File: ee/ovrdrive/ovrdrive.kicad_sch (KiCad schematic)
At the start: 48 parts, among them J1 USB_A, J2 Conn_01x02_Female, Q1 RU1J002YNTCL, U1 SM3257ENT, U2 FLASH, U3 ATtiny24A-MM, U4 74AUC1G32, U5 LMV321, U6 LM4040DBZ-2.5

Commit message: Added some datasheets made some changes to the boards.
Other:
- note removed: "Open Questions 1. Where does DQS0 from U1 wire to? 2. U1-P44, wired to 680R resistor in design guide."
- moved on the sheet: C18
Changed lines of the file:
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@@
     (stroke (width 0) (type default) (color 0 0 0 0))
   )
-  (wire (pts (xy 204.47 81.915) (xy 204.47 82.55))
+  (wire (pts (xy 213.36 80.645) (xy 213.36 81.28))
     (stroke (width 0) (type default) (color 0 0 0 0))
   )
@@
     (stroke (width 0) (type default) (color 0 0 0 0))
   )
+  (wire (pts (xy 165.735 68.58) (xy 154.94 68.58))
+    (stroke (width 0) (type default) (color 0 0 0 0))
+  )
   (wire (pts (xy 54.61 88.9) (xy 52.705 88.9))
     (stroke (width 0) (type default) (color 0 0 0 0))
@@
     (stroke (width 0) (type default) (color 0 0 0 0))
   )
-  (wire (pts (xy 204.47 76.2) (xy 204.47 76.835))
+  (wire (pts (xy 213.36 74.93) (xy 213.36 75.565))
     (stroke (width 0) (type default) (color 0 0 0 0))
   )
@@
     (stroke (width 0) (type default) (color 0 0 0 0))
   )
+  (wire (pts (xy 236.22 139.065) (xy 236.22 140.335))
+    (stroke (width 0) (type default) (color 0 0 0 0))
+  )
+  (wire (pts (xy 170.18 85.725) (xy 173.355 85.725))
+    (stroke (width 0) (type default) (color 0 0 0 0))
+  )
+  (wire (pts (xy 60.96 59.055) (xy 60.96 60.96))
+    (stroke (width 0) (type default) (color 0 0 0 0))
+  )
+  (wire (pts (xy 43.18 88.9) (xy 52.705 88.9))
+    (stroke (width 0) (type default) (color 0 0 0 0))
+  )
+  (wire (pts (xy 100.965 38.1) (xy 100.965 39.37))
+    (stroke (width 0) (type default) (color 0 0 0 0))
+  )
+  (wire (pts (xy 85.725 157.48) (xy 85.725 159.385))
+    (stroke (width 0) (type default) (color 0 0 0 0))
+  )
+  (wire (pts (xy 84.455 62.865) (xy 82.55 62.865))
+    (stroke (width 0) (type default) (color 0 0 0 0))
+  )
+  (wire (pts (xy 236.22 146.685) (xy 236.22 148.59))
+    (stroke (width 0) (type default) (color 0 0 0 0))
+  )
   (wire (pts (xy 165.735 57.785) (xy 165.735 68.58))
     (stroke (width 0) (type default) (color 0 0 0 0))
   )
-  (wire (pts (xy 236.22 139.065) (xy 236.22 140.335))
-    (stroke (width 0) (type default) (color 0 0 0 0))
-  )
-  (wire (pts (xy 170.18 85.725) (xy 173.355 85.725))
-    (stroke (width 0) (type default) (color 0 0 0 0))
-  )
-  (wire (pts (xy 60.96 59.055) (xy 60.96 60.96))
-    (stroke (width 0) (type default) (color 0 0 0 0))
-  )
-  (wire (pts (xy 43.18 88.9) (xy 52.705 88.9))
-    (stroke (width 0) (type default) (color 0 0 0 0))
-  )
-  (wire (pts (xy 100.965 38.1) (xy 100.965 39.37))
-    (stroke (width 0) (type default) (color 0 0 0 0))
-  )
-  (wire (pts (xy 85.725 157.48) (xy 85.725 159.385))
-    (stroke (width 0) (type default) (color 0 0 0 0))
-  )
-  (wire (pts (xy 84.455 62.865) (xy 82.55 62.865))
-    (stroke (width 0) (type default) (color 0 0 0 0))
-  )
-  (wire (pts (xy 236.22 146.685) (xy 236.22 148.59))
-    (stroke (width 0) (type default) (color 0 0 0 0))
-  )
   (wire (pts (xy 170.18 87.63) (xy 173.355 87.63))
     (stroke (width 0) (type default) (color 0 0 0 0))
@@
   )
   (wire (pts (xy 143.51 74.93) (xy 143.51 76.2))
-    (stroke (width 0) (type default) (color 0 0 0 0))
-  )
-  (wire (pts (xy 165.735 68.58) (xy 154.94 68.58))
     (stroke (width 0) (type default) (color 0 0 0 0))
   )
@@
   (text "Connect\nRx here" (at 214.63 141.605 180)
     (effects (font (size 1.27 1.27)) (justify right bottom))
-  )
-  (text "Open Questions\n1. Where does DQS0 from U1 wire to?\n2. U1-P44, wired to 680R resistor in design guide."
-    (at 154.94 130.81 0)
-    (effects (font (size 1.27 1.27)) (justify left bottom))
   )
   (text "Rx = Vs * (R2/2.5)\nWhere U6 is a 2.5V\nregulator." (at 251.46 138.43 0)
@@
     (pin "2")
   )
-  (symbol (lib_id "power:+3.3V") (at 204.47 76.2 0) (unit 1)
-    (in_bom yes) (on_board yes) (fields_autoplaced)
-    (property "Reference" "#PWR026" (id 0) (at 204.47 80.01 0)
-      (effects (font (size 1.27 1.27)) hide)
-    )
-    (property "Value" "+3.3V" (id 1) (at 204.47 72.6242 0))
-    (property "Footprint" "" (id 2) (at 204.47 76.2 0)
-      (effects (font (size 1.27 1.27)) hide)
-    )
-    (property "Datasheet" "" (id 3) (at 204.47 76.2 0)
+  (symbol (lib_id "power:+3.3V") (at 213.36 74.93 0) (unit 1)
+    (in_bom yes) (on_board yes) (fields_autoplaced)
+    (property "Reference" "#PWR026" (id 0) (at 213.36 78.74 0)
+      (effects (font (size 1.27 1.27)) hide)
+    )
+    (property "Value" "+3.3V" (id 1) (at 213.36 71.3542 0))
+    (property "Footprint" "" (id 2) (at 213.36 74.93 0)
+      (effects (font (size 1.27 1.27)) hide)
+    )
+    (property "Datasheet" "" (id 3) (at 213.36 74.93 0)
       (effects (font (size 1.27 1.27)) hide)
     )
@@
     (pin "1")
   )
-  (symbol (lib_id "power:GND") (at 204.47 82.55 0) (unit 1)
-    (in_bom yes) (on_board yes) (fields_autoplaced)
-    (property "Reference" "#PWR027" (id 0) (at 204.47 88.9 0)
-      (effects (font (size 1.27 1.27)) hide)
-    )
-    (property "Value" "GND" (id 1) (at 204.47 86.9934 0)
-      (effects (font (size 1.27 1.27)) hide)
-    )
-    (property "Footprint" "" (id 2) (at 204.47 82.55 0)
-      (effects (font (size 1.27 1.27)) hide)
-    )
-    (property "Datasheet" "" (id 3) (at 204.47 82.55 0)
+  (symbol (lib_id "power:GND") (at 213.36 81.28 0) (unit 1)
+    (in_bom yes) (on_board yes) (fields_autoplaced)
+    (property "Reference" "#PWR027" (id 0) (at 213.36 87.63 0)
+      (effects (font (size 1.27 1.27)) hide)
+    )
+    (property "Value" "GND" (id 1) (at 213.36 85.7234 0)
+      (effects (font (size 1.27 1.27)) hide)
+    )
+    (property "Footprint" "" (id 2) (at 213.36 81.28 0)
+      (effects (font (size 1.27 1.27)) hide)
+    )
+    (property "Datasheet" "" (id 3) (at 213.36 81.28 0)
       (effects (font (size 1.27 1.27)) hide)
     )
@@
     (pin "1")
   )
-  (symbol (lib_id "Device:C_Small") (at 204.47 79.375 0) (unit 1)
-    (in_bom yes) (on_board yes)
-    (property "Reference" "C18" (id 0) (at 203.2 77.47 0)
-      (effects (font (size 1.27 1.27)) (justify right))
-    )
-    (property "Value" "100nF" (id 1) (at 203.835 81.28 0)
-      (effects (font (size 1.27 1.27)) (justify right))
-    )
-    (property "Footprint" "Capacitor_SMD:C_0603_1608Metric" (id 2) (at 204.47 79.375 0)
-      (effects (font (size 1.27 1.27)) hide)
-    )
-    (property "Datasheet" "~" (id 3) (at 204.47 79.375 0)
-      (effects (font (size 1.27 1.27)) hide)
-    )
+  (symbol (lib_id "Device:C_Small") (at 213.36 78.105 0) (unit 1)
+    (in_bom yes) (on_board yes)
+    (property "Reference" "C18" (id 0) (at 212.09 76.2 0)
+      (effects (font (size 1.27 1.27)) (justify right))
+    )
+    (property "Value" "100nF" (id 1) (at 212.725 80.01 0)
+      (effects (font (size 1.27 1.27)) (justify right))
+    )
+    (property "Footprint" "Capacitor_SMD:C_0603_1608Metric" (id 2) (at 213.36 78.105 0)
+      (effects (font (size 1.27 1.27)) hide)
+    )
+    (property "Datasheet" "~" (id 3) (at 213.36 78.105 0)
+      (effects (font (size 1.27 1.27)) hide)
+    )

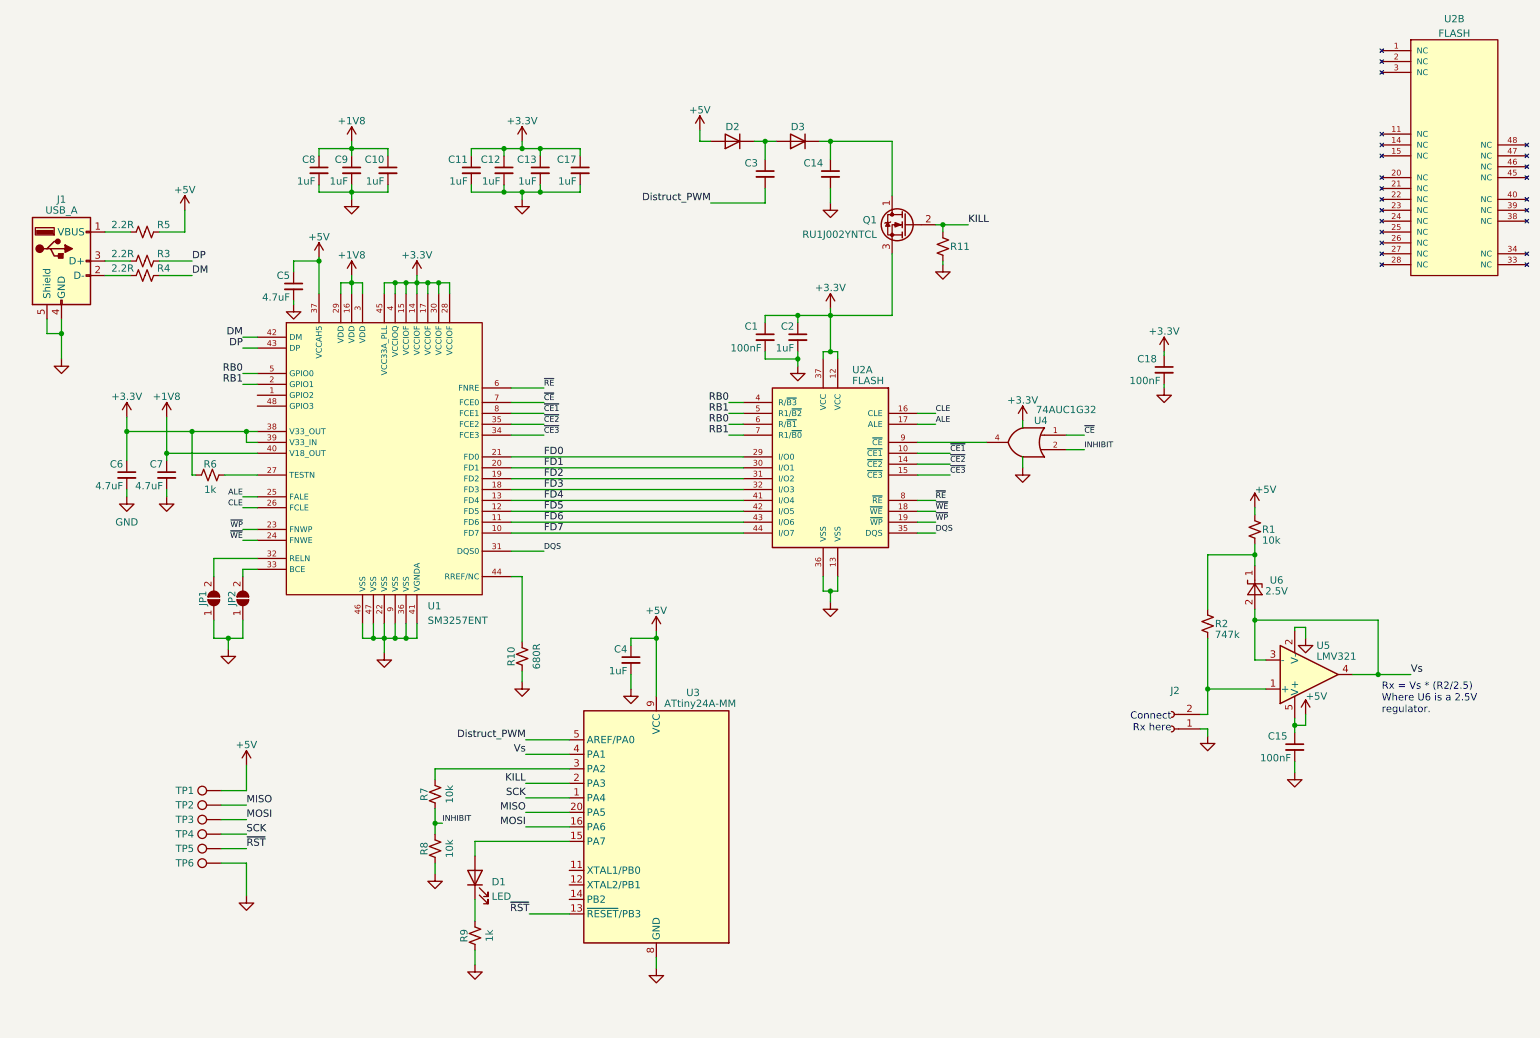
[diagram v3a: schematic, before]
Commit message: Removed analog circuitry for spit detection, shortened entire board by 0.6mm to fit in enclosure.
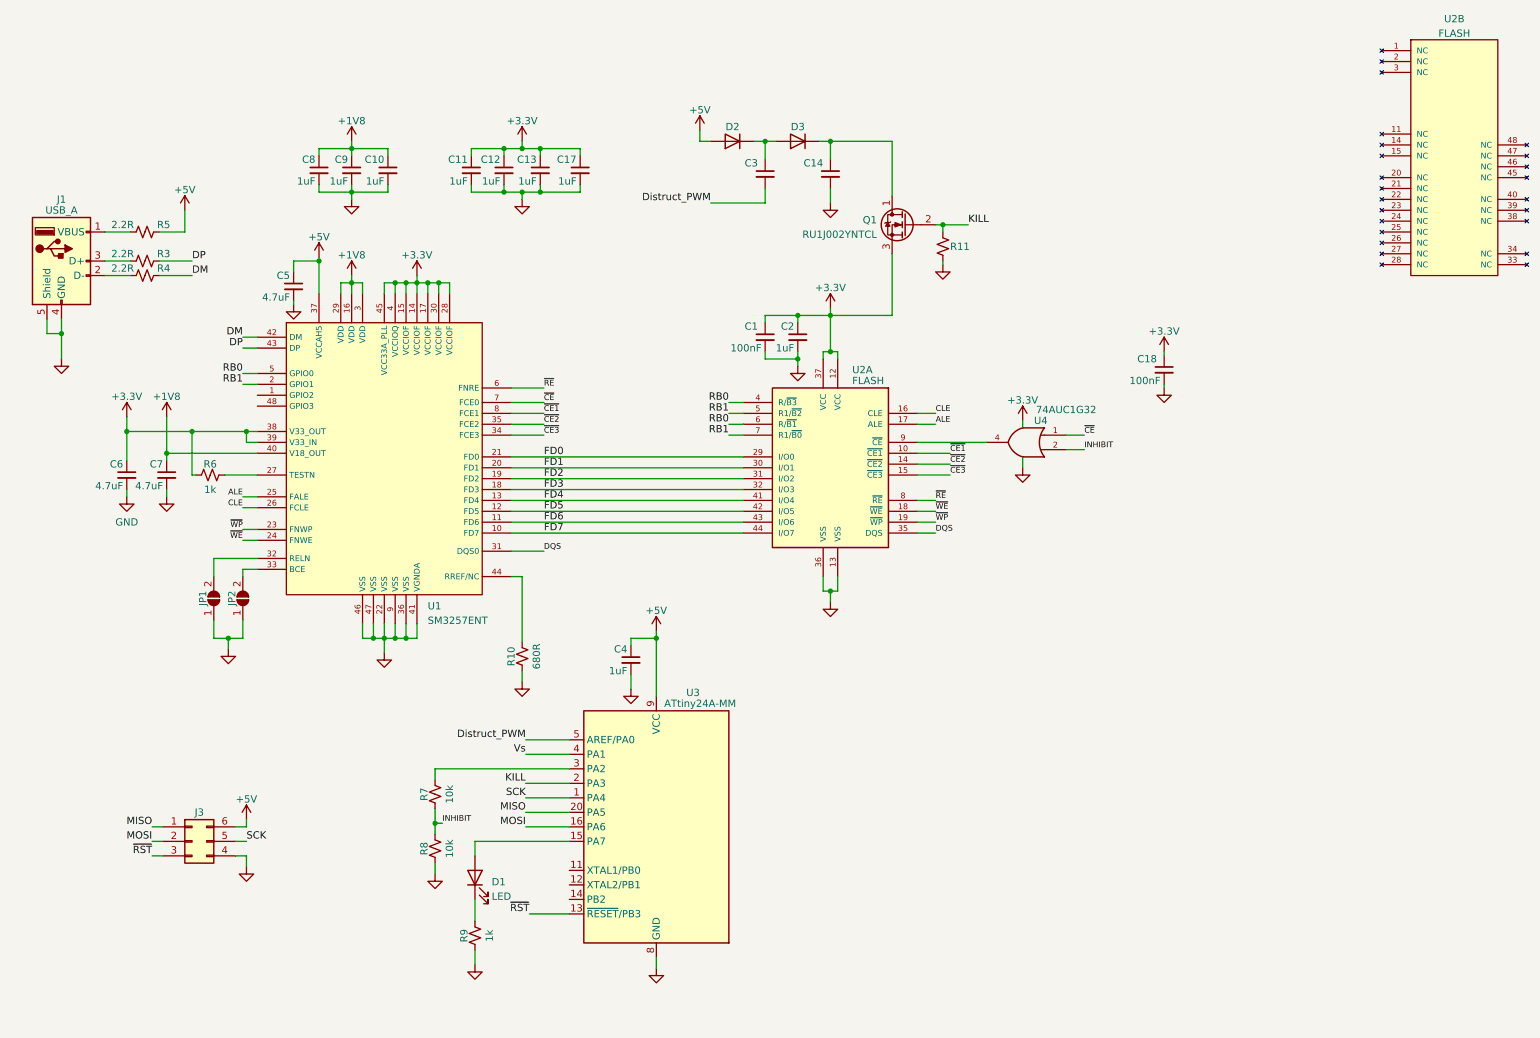
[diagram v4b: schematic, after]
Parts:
- removed C15: 100nF, Capacitor_SMD:C_0603_1608Metric, symbol Device:C_Small
- removed J2: Conn_01x02_Female, symbol Connector:Conn_01x02_Female
- removed R1: 10k, Resistor_SMD:R_0603_1608Metric, symbol Device:R_Small_US
- removed R2: 747k, Resistor_SMD:R_0603_1608Metric, symbol Device:R_Small_US
- removed TP1, TP2, TP3, TP4, TP5, TP6: TestPoint, TestPoint:TestPoint_Pad_1.0x1.0mm, symbol Connector:TestPoint
- removed U5: LMV321, Package_TO_SOT_SMD:SOT-23-5, symbol Amplifier_Operational:LMV321
- removed U6: LM4040DBZ-2.5, Package_TO_SOT_SMD:SOT-23, symbol Reference_Voltage:LM4040DBZ-2.5
- added J3: Conn_02x03_Counter_Clockwise, Connector_PinHeader_1.27mm:PinHeader_2x03_P1.27mm_Horizontal, symbol Connector_Generic:Conn_02x03_Counter_Clockwise
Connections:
- net +5V: now also J3.6 (Pin_6)
- net GND: now also J3.4 (Pin_4)
- net MISO: now also J3.1 (Pin_1)
- net MOSI: now also J3.2 (Pin_2)
- net SCK: now also J3.5 (Pin_5)
- net ~{RST}: now also J3.3 (Pin_3)
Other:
- note removed: "Connect Rx here"
- note removed: "Rx = Vs * (R2/2.5) Where U6 is a 2.5V regulator."

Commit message: Changes components and a leftover commit.
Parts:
- removed D2, D3: D, Diode_SMD:D_0603_1608Metric, symbol Device:D
- removed Q1: RU1J002YNTCL, Package_TO_SOT_SMD:SOT-23, symbol Device:Q_NMOS_DGS
- added C15: 22uF, Capacitor_SMD:C_0603_1608Metric, symbol Device:C_Small
- added D2, D3, D4: D_Schottky, Diode_SMD:D_0603_1608Metric, symbol Device:D_Schottky
- added Q1, Q2: SSM3J328R,LF, Package_TO_SOT_SMD:SOT-23, symbol Device:Q_PMOS_GSD
- added Q3: DMG1012TQ-7, Package_TO_SOT_SMD:SOT-523, symbol Device:Q_NMOS_GSD
- added R1, R12: 1k, Resistor_SMD:R_0402_1005Metric, symbol Device:R_Small_US
- added R13: 220R, Resistor_SMD:R_0603_1608Metric, symbol Device:R_Small_US
- added R2: 10k, Resistor_SMD:R_0402_1005Metric, symbol Device:R_Small_US
- added TH1: 10k, Resistor_SMD:R_0603_1608Metric, symbol Device:Thermistor_NTC
- added TP1, TP2: TestPoint, TestPoint:TestPoint_Pad_D1.0mm, symbol Connector:TestPoint
- C1, C18, C3: MPN (none) -> CC0603KRX7R7BB104
- C10, C11, C12, C13, C17, C2, C4, C8, C9: MPN (none) -> CC0603KRX7R7BB105
- C14: value 100nF -> 22uF; MPN (none) -> CL10A226MO7JZNC
- C5, C6, C7: MPN (none) -> CL10A475KP8NNNC
- J3: MPN (none) -> 20021112-00006T4LF; now left out of the parts list
- JP1, JP2: now left out of the parts list
- R10: MPN (none) -> RC0603FR-07680RL
- R11: value 2.2R -> 1k; footprint Resistor_SMD:R_0603_1608Metric -> Resistor_SMD:R_0402_1005Metric; MPN (none) -> RC0402FR-071KL
- R3, R4, R5: MPN RK73B1JTTD2R2J -> RC0603FR-072R2L
- R6: MPN (none) -> RC0603FR-071KL
- R7, R8: footprint Resistor_SMD:R_0603_1608Metric -> Resistor_SMD:R_0402_1005Metric; MPN (none) -> RC0402FR-0710KL
- R9: footprint Resistor_SMD:R_0603_1608Metric -> Resistor_SMD:R_0402_1005Metric; MPN (none) -> RC0402FR-071KL
- U1: MPN (none) -> SM3257ENT
- U2: MPN (none) -> K9HDG08U1A
- U3: MPN (none) -> ATTINY24A-MMHR
- U4: value 74AUC1G32 -> SN74LVC1G32DCKR; MPN SN74AUC1G32DBVR -> SN74LVC1G32DCKR
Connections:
- net +3.3V: now also D4.2 (A); no longer C1.1, C2.1, U2.12 (VCC), U2.37 (VCC)
- net +5V: now also J3.1 (Pin_1), D2.2 (A), Q1.2 (S), R12.2, TH1.1; no longer J3.6 (Pin_6)
- net GND: now also C15.2, Q3.2 (S), R1.1, R13.1, R2.1; no longer R11.1
- net KILL: now also Q3.1 (G), R1.2; no longer R11.2
- net MISO: now also J3.6 (Pin_6); no longer J3.1 (Pin_1)
- net at C14.1: now also R11.2, C15.1, D3.1 (K), Q2.2 (S)
- net PB0: now reaches U3.11 (XTAL1/PB0)
- net PB0: now also TP1.1
- net PB1: now reaches U3.12 (XTAL2/PB1)
- net PB1: now also TP2.1
- net PB2: now reaches U3.14 (PB2)
- net PB2: now also Q1.1 (G), R12.1
- net at C3.1: now also D2.1 (K), D3.2 (A)
- net Vs renamed PA1
- net PA1: now also R2.2, TH1.2
- new net: Q2.1 (G), Q3.3 (D), R11.1
- new net: Q1.3 (D), R13.2
- new net: C1.1, C2.1, D4.1 (K), Q2.3 (D), U2.12 (VCC), U2.37 (VCC)
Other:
- note added: "Heater"
- moved on the sheet: C14, C18, C3, D1, J3, R11, R9

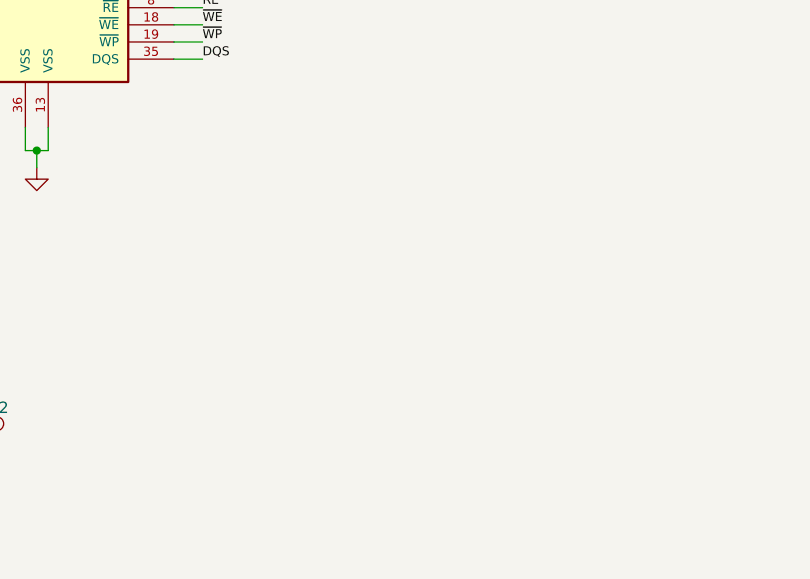
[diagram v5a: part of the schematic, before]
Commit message: Added config files that are working for the new flash.
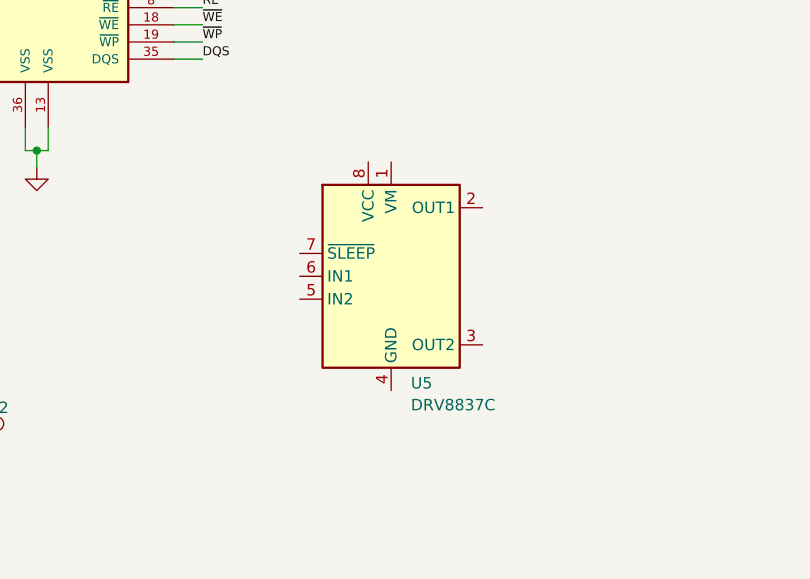
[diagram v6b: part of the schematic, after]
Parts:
- added U5: DRV8837C, Package_SON:WSON-8-1EP_2x2mm_P0.5mm_EP0.9x1.6mm, symbol Driver_Motor:DRV8837C
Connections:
- new net: U5.4 (GND), U5.9 (GND)
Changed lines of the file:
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@@
+    )
+  )
+  (symbol (lib_id "Driver_Motor:DRV8837C") (at 194.31 130.81 0) (unit 1)
+    (in_bom yes) (on_board yes) (dnp no) (fields_autoplaced)
+    (property "Reference" "U5" (at 196.5041 142.6901 0)
+      (effects (font (size 1.27 1.27)) (justify left))
+    )
+    (property "Value" "DRV8837C" (at 196.5041 145.1143 0)
+      (effects (font (size 1.27 1.27)) (justify left))
+    )
+    (property "Footprint" "Package_SON:WSON-8-1EP_2x2mm_P0.5mm_EP0.9x1.6mm" (at 194.31 152.4 0)
+      (effects (font (size 1.27 1.27)) hide)
+    )
+    (property "Datasheet" "http://www.ti.com/lit/ds/symlink/drv8837c.pdf" (at 194.31 130.81 0)
+      (effects (font (size 1.27 1.27)) hide)
+    )
+    (pin "1")
+    (pin "2")
+    (pin "3")
+    (pin "4")
+    (pin "5")
+    (pin "6")
+    (pin "7")
+    (pin "8")
+    (pin "9")
+    (instances
+      (project "ovrdrive"
+        (path "/73c7e5ea-07c9-44ef-a9f8-630a9b8be271"
+          (reference "U5") (unit 1)
+        )
+      )
     )
   )
